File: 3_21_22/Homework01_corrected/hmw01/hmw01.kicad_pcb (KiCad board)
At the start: 2 copper layers, 50 x 68 mm, 43 parts, among them J1 I2C Connector, J2 USB_B_Micro, J3 Address Connector, J4 Vibration Motor Connect, J5 UART Connector, J6 CS Connector, Q1 SS8050, SW1 Resetbutton, SW2 Userbutton, U1 uPD25608, U2 PIC18F4550-IPT, U3 74HC14, U4 74HC00, U5 74HC14, Y1 4MHz

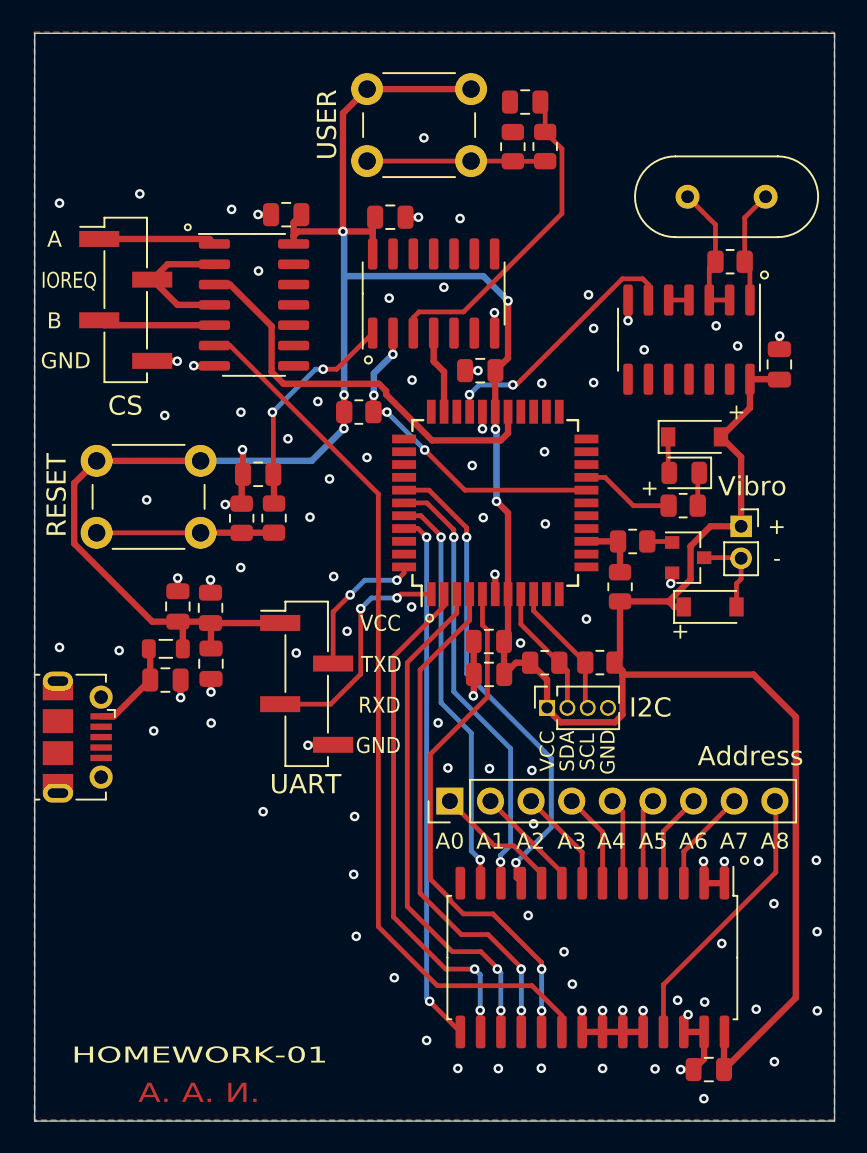
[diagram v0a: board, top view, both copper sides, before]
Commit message: Added missing ground
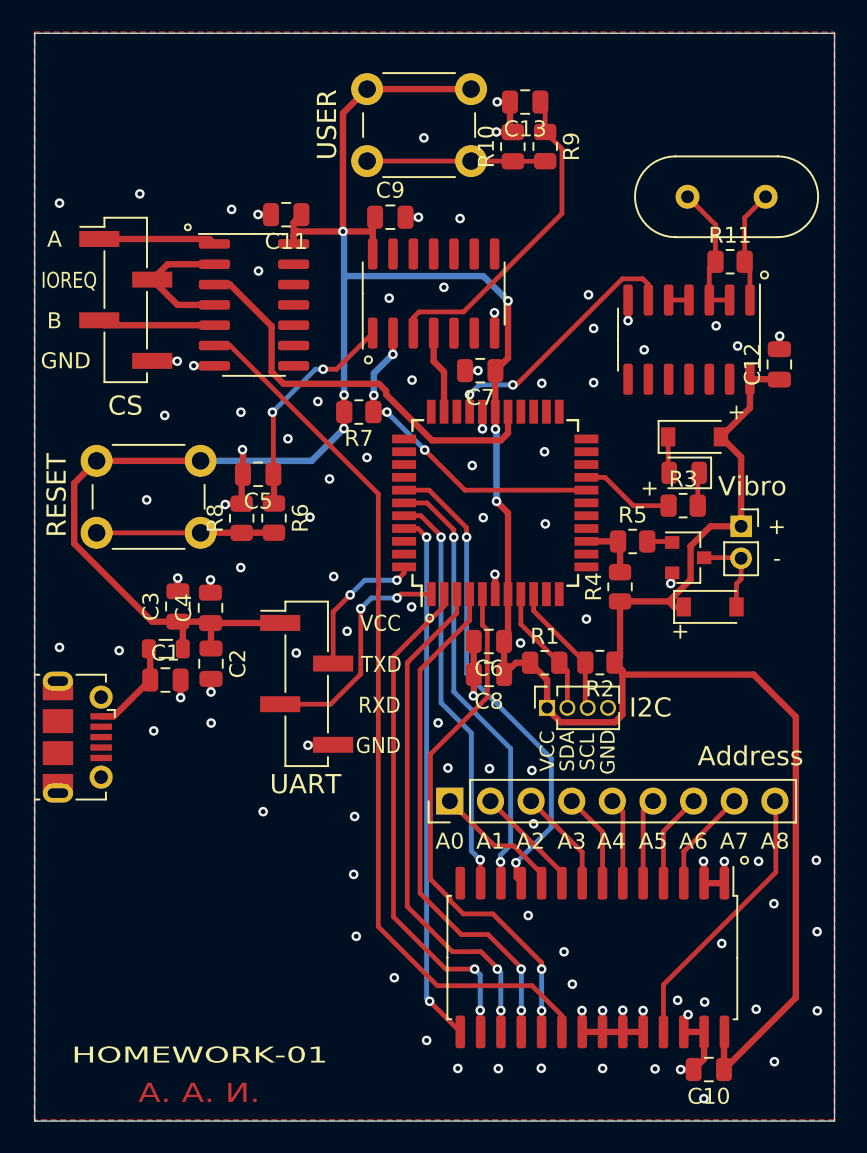
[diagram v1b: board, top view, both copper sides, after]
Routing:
- net GND: track 44.2 -> 48.0 mm, vias 96 -> 98
